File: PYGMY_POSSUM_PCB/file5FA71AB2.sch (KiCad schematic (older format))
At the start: 3 parts, among them J3 AudioJack3_Ground_SwitchTR, U5 PS2501-1

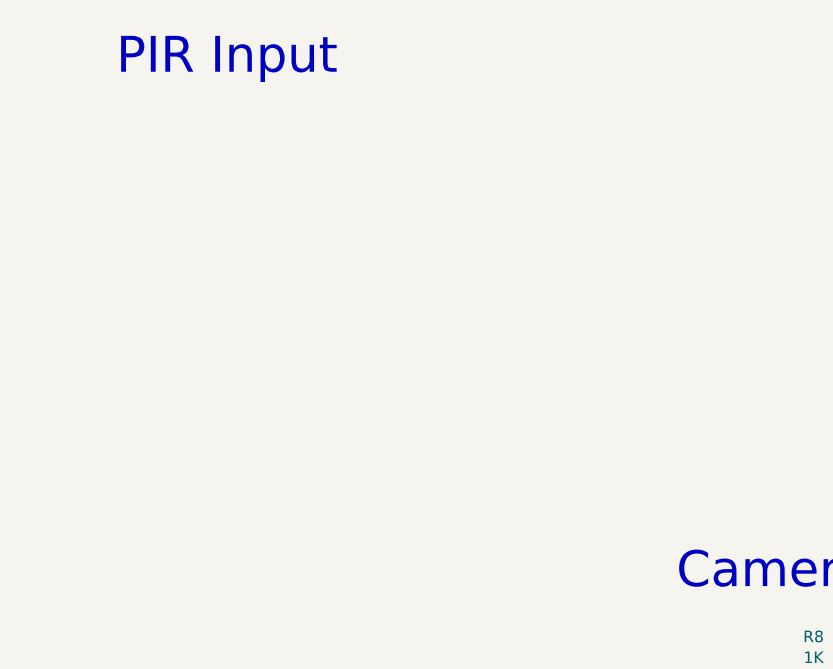
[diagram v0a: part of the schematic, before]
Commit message: added bulk of components
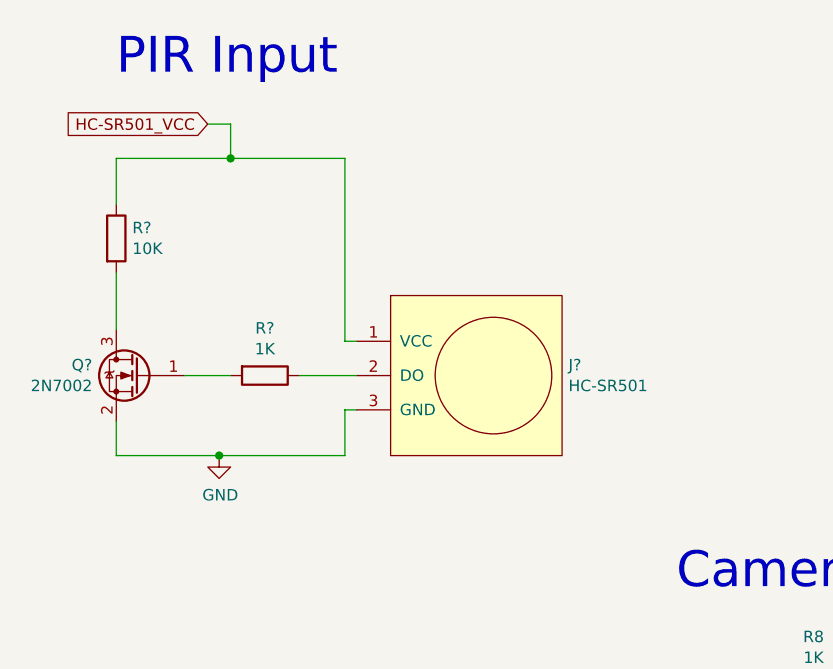
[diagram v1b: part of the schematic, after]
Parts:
- added J?: HC-SR501, PIC_CAM_TRAP:HC-SR501, symbol BANKSIA_BYTES_SYMBOLS:HC-SR501
- added Q?: 2N7002, Package_TO_SOT_SMD:SOT-23, symbol Transistor_FET:2N7002
- added R?: 1K, symbol Device:R
- added R?: 10K, symbol Device:R
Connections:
- net GND: now also J?.3 (GND), Q?.2 (S)
- new net: J?.2 (DO), R?.1
- new net: Q?.1 (G), R?.2
- new net: Q?.3 (D), R?.2
- new net HC-SR501_VCC: J?.1 (VCC), R?.1
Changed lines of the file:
@@
 Text Notes 3550 3650 0    157  ~ 0
 Camera Output
+$Comp
+L BANKSIA_BYTES_SYMBOLS:HC-SR501 J?
+U 1 1 5FACBABF
+P 2350 2700
+F 0 "J?" H 3078 2746 50  0000 L CNN
+F 1 "HC-SR501" H 3078 2655 50  0000 L CNN
+F 2 "PIC_CAM_TRAP:HC-SR501" H 2350 2700 50  0001 C CNN
+F 3 "~" H 2350 2700 50  0001 C CNN
+	1    2350 2700
+	1    0    0    -1
+$EndComp
+$Comp
+L power:GND #PWR?
+U 1 1 5FACBEA3
+P 1550 3050
+F 0 "#PWR?" H 1550 2800 50  0001 C CNN
+F 1 "GND" H 1555 2877 50  0000 C CNN
+F 2 "" H 1550 3050 50  0001 C CNN
+F 3 "" H 1550 3050 50  0001 C CNN
+	1    1550 3050
+	1    0    0    -1
+$EndComp
+Wire Wire Line
+	2150 2850 2100 2850
+$Comp
+L Device:R R?
+U 1 1 5FACC820
+P 1750 2700
+F 0 "R?" V 1543 2700 50  0000 C CNN
+F 1 "1K" V 1634 2700 50  0000 C CNN
+F 2 "" V 1680 2700 50  0001 C CNN
+F 3 "~" H 1750 2700 50  0001 C CNN
+	1    1750 2700
+	0    1    1    0
+$EndComp
+Text GLabel 1500 1600 0    50   Input ~ 0
+HC-SR501_VCC
+$Comp
+L Device:R R?
+U 1 1 5FACFB58
+P 1100 2100
+F 0 "R?" H 1170 2146 50  0000 L CNN
+F 1 "10K" H 1170 2055 50  0000 L CNN
+F 2 "" V 1030 2100 50  0001 C CNN
+F 3 "~" H 1100 2100 50  0001 C CNN
+	1    1100 2100
+	1    0    0    -1
+$EndComp
+Wire Wire Line
+	1100 1750 1100 1950
+Wire Wire Line
+	1100 3050 1550 3050
+Connection ~ 1550 3050
+Wire Wire Line
+	1100 2250 1100 2500
+Wire Wire Line
+	1600 1750 1600 1600
+Wire Wire Line
+	1600 1600 1500 1600
+Connection ~ 1600 1750
+Wire Wire Line
+	1600 1750 1100 1750
+Wire Wire Line
+	2100 1750 2100 2550
+Wire Wire Line
+	2100 2550 2150 2550
+Wire Wire Line
+	2100 2850 2100 3050
+Wire Wire Line
+	1550 3050 2100 3050
+Wire Wire Line
+	1600 1750 2100 1750
+$Comp
+L Transistor_FET:2N7002 Q?
+U 1 1 5FAD747B
+P 1200 2700
+F 0 "Q?" H 1405 2746 50  0000 L CNN
+F 1 "2N7002" H 1405 2655 50  0000 L CNN
+F 2 "Package_TO_SOT_SMD:SOT-23" H 1400 2625 50  0001 L CIN
+F 3 "https://www.fairchildsemi.com/datasheets/2N/2N7002.pdf" H 1200 2700 50  0001 L CNN
+	1    1200 2700
+	-1   0    0    -1
+$EndComp
+Wire Wire Line
+	1100 2900 1100 3050
+Wire Wire Line
+	1900 2700 2150 2700
+Wire Wire Line
+	1600 2700 1400 2700
 $EndSCHEMATC
